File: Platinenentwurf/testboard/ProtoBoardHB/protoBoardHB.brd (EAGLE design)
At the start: 73.3 x 76.2 mm, 50 parts, among them IC1 CD74HCT125M, J1 M20-9980545, J2 M20-9980545, Q1 SMMBT3904WT1G, U2 STM32F4X5RG

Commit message: änderungen Platine + Bestellliste
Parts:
- added J3, J4: M20-9990246, SamacSys_Parts:HDRV2W64P0X254_1X2_508X254X864
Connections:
- new net N$2: HB_2.6, J3.2
- new net N$7: HB_1.6, J4.1
- net IS_1: now also J4.2; no longer HB_1.6
- net IS_2: now also J3.1; no longer HB_2.6
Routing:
- net GND: track 427.1 -> 482.9 mm, vias 8 -> 13
- net N$7: track 0.00 -> 24.3 mm, vias 0 -> 1
- net N$2: track 0.00 -> 23.4 mm, vias 0 -> 1
- net IS_1: track 75.8 -> 90.4 mm, vias 3 -> 2
- net IS_2: track 63.4 -> 67.3 mm, vias 3 -> 2

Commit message: update Platine
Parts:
- removed CAN_CONNECTION: 282836-2, SamacSys_Parts:SHDR2W100P0X500_1X2_1000X820X1
- removed C_HB_VS_1, C_HB_VS_2: 0.47uF, adafruit:C1206
- removed C_Q_1, C_Q_2: 22pF, adafruit:C0805
- removed C_VCAP_1, C_VCAP_2: 2.2uF, adafruit:C1206
- removed C_VDDA, C_VDD_1, C_VDD_2, C_VDD_3, C_VDD_4: 100nF, adafruit:C1206
- removed C_VDD_47: 4.7nF, adafruit:C1206
- removed C_VR33_VIN, C_VR5_VIN: 1uF, adafruit:C1206
- removed C_VR33_VO1, C_VR5_VO1: 4.7uF, adafruit:C1206
- removed IC1: CD74HCT125M, SamacSys_Parts:SOIC127P600X175-14N
- removed J1, J2: M20-9980545, SamacSys_Parts:HDRV10W80P254_2X5_1270X508X864
- removed J3, J4: M20-9990246, SamacSys_Parts:HDRV2W64P0X254_1X2_508X254X864
- removed QUARZ: ABLS-8.000MHZ-K4T, SamacSys_Parts:ABLS-12.000MHZ-B2
- removed R_CD: 1K, adafruit:R1206
- removed R_HB_INH_1, R_HB_INH_2, R_HB_IN_1, R_HB_IN_2: 10K, adafruit:R1206
- removed R_HB_IS_1, R_HB_IS_2: 1k, adafruit:R1206
- removed R_SMM_1, R_SMM_2: 100K, adafruit:R1206
- removed VREG_55: LDL1117S50R, SamacSys_Parts:SOT230P700X180-4N
- added C1, C3: 4.7uF, adafruit:C1206
- added C10, C12, C7, C8, C9: 100nF, adafruit:C1206
- added C11: 4.7nF, adafruit:C1206
- added C2, C4: 1uF, adafruit:C1206
- added C5, C6: 2.2uF, adafruit:C1206
- added CAN_OUT: 282836-2, SamacSys_Parts:SHDR2W100P0X500_1X2_1000X820X1
- added CD74HCT: CD74HCT125M, SamacSys_Parts:SOIC127P600X175-14N
- added CH1, CH2: 0.47uF, adafruit:C1206
- added CQ1, CQ2: 22pF, adafruit:C0805
- added J_CD, SENSORIK: M20-9980545, SamacSys_Parts:HDRV10W80P254_2X5_1270X508X864
- added J_IS1, J_IS2: M20-9990246, SamacSys_Parts:HDRV2W64P0X254_1X2_508X254X864
- added QUARTZ: ABLS-8.000MHZ-K4T, SamacSys_Parts:ABLS-12.000MHZ-B2
- added R10, R11, R12, R13: 10K, adafruit:R1206
- added R14, R9: 1k, adafruit:R1206
- added R15: 1K, adafruit:R1206
- added R16: 100K, adafruit:R1206
- added R17: 7.5K, adafruit:R1206
- added VREG_5: LDL1117S50R, SamacSys_Parts:SOT230P700X180-4N
- moved C_CAN 2.01 mm to (64.1, 34.9)
- moved CAN_T 2.01 mm to (64.1, 29.8)
- moved Q1 2.01 mm to (64.1, 17.1)
- moved HB_1 2.01 mm to (13.3, 52.7)
- moved U2 2.01 mm to (52.7, 34.9)
- moved BAT 2.01 mm to (8.26, 38.7)
- moved HB_ST 2.01 mm to (45.1, 56.5)
- moved R3 2.01 mm to (45.1, 23.5)
- moved R4 2.01 mm to (47.6, 23.5)
- moved R5 2.01 mm to (50.2, 23.5)
- moved R6 2.01 mm to (52.7, 23.5)
- moved SWD 2.01 mm to (69.2, 59.1)
- moved HB_2 2.01 mm to (29.8, 52.7)
- moved R1 2.01 mm to (31.1, 17.1)
- moved R2 2.01 mm to (28.6, 17.1)
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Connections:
- removed net N$16: J2.8
- removed net N$17: J2.10
- net CANH: now also CAN_OUT.1; no longer CAN_CONNECTION.1
- net CANL: now also CAN_OUT.2; no longer CAN_CONNECTION.2
- net CD_EN: now also CD74HCT.1, CD74HCT.13, CD74HCT.4, J_CD.7, J_CD.9; no longer IC1.1, IC1.13, IC1.4, J1.7, J1.9
- net CD_VCC: now also CD74HCT.14, J_CD.1, J_CD.3; no longer IC1.14, J1.1, J1.3
- net GND: now also C1.2, C10.2, C11.2, C12.2, C2.2, C3.1, C4.1, C5.2, C6.2, C7.2, C8.2, C9.2, CD74HCT.7, CH1.2, CH2.2, CQ1.2, CQ2.2, R14.1, R15.1, R17.2, R9.1, SENSORIK.4, VREG_5.1; no longer C_HB_VS_1.2, C_HB_VS_2.2, C_Q_1.2, C_Q_2.2, C_VCAP_1.2, C_VCAP_2.2, C_VDDA.2, C_VDD_1.2, C_VDD_2.2, C_VDD_3.2, C_VDD_4.2, C_VDD_47.2, C_VR33_VIN.2, C_VR33_VO1.2, C_VR5_VIN.1, C_VR5_VO1.1, IC1.7, J2.4, R_CD.1, R_HB_IS_1.1, R_HB_IS_2.1, R_SMM_2.2, VREG_55.1
- net INH: now also CD74HCT.11, R11.1, R12.1; no longer IC1.11, R_HB_INH_1.1, R_HB_INH_2.1
- net INH_M: now also CD74HCT.12; no longer IC1.12
- net IN_1: now also CD74HCT.6, R13.1; no longer IC1.6, R_HB_IN_1.1
- net IN_2: now also CD74HCT.3, R10.1; no longer IC1.3, R_HB_IN_2.1
- net IN_M_1: now also CD74HCT.5; no longer IC1.5
- net IN_M_2: now also CD74HCT.2; no longer IC1.2
- net IS_1: now also J_IS1.2, R14.2; no longer J4.2, R_HB_IS_1.2
- net IS_2: now also J_IS2.1, R9.2; no longer J3.1, R_HB_IS_2.2
- net N$1: now also J_CD.10, R15.2; no longer J1.10, R_CD.2
- net N$15: now also SENSORIK.6; no longer J2.6
- net N$2: now also J_IS2.2; no longer J3.2
- net N$3: now also R13.2; no longer R_HB_IN_1.2
- net N$4: now also R12.2; no longer R_HB_INH_1.2
- net N$5: now also R10.2; no longer R_HB_IN_2.2
- net N$6: now also R11.2; no longer R_HB_INH_2.2
- net N$7: now also J_IS1.1; no longer J4.1
- net OSC_IN: now also CQ2.1, QUARTZ.2; no longer C_Q_2.1, QUARZ.2
- net OSC_OUT: now also CQ1.1, QUARTZ.1; no longer C_Q_1.1, QUARZ.1
- net OUT_PA4: now also SENSORIK.7; no longer J2.7
- net OUT_PA5: now also SENSORIK.3; no longer J2.3
- net OUT_PA6: now also SENSORIK.5; no longer J2.5
- net OUT_PB1: now also SENSORIK.1; no longer J2.1
- net PA8: now also R16.2; no longer R_SMM_1.2
- net SS_VN: now also R17.1, SENSORIK.2; no longer J2.2, R_SMM_2.1
- net V12: now also C2.1, C4.2, CH1.1, CH2.1, VREG_5.3; no longer C_HB_VS_1.1, C_HB_VS_2.1, C_VR33_VIN.1, C_VR5_VIN.2, VREG_55.3
- net V33: now also C1.1, C10.1, C11.1, C12.1, C5.1, C6.1, C7.1, C8.1, C9.1, CD74HCT.10, J_CD.2, J_CD.8, R16.1, SENSORIK.9; no longer C_VCAP_1.1, C_VCAP_2.1, C_VDDA.1, C_VDD_1.1, C_VDD_2.1, C_VDD_3.1, C_VDD_4.1, C_VDD_47.1, C_VR33_VO1.1, IC1.10, J1.2, J1.8, J2.9, R_SMM_1.1
- net V5: now also C3.2, J_CD.4, VREG_5.4; no longer C_VR5_VO1.2, J1.4, VREG_55.4
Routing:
- net GND: track 482.9 -> 495.0 mm, vias 13 -> 15
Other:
- board text added: "CD_EN"
- board text added: "CD_VCC"
- board text added: "GND"
- board text added: "INH_EXT"
- board text added: "IN_M_1"
- board text added: "IN_M_2"
- board text added: "IS_1"
- board text added: "IS_2"
- board text added: "NRST"
- board text added: "NU"
- board text added: "OUT_PA4"
- board text added: "OUT_PA5"
- board text added: "OUT_PA6"
- board text added: "OUT_PB1"
- board text added: "Protoboard"
- board text added: "SS_VN"
- board text added: "SWCLK"
- board text added: "SWDIO"
- board text added: "TRACESWO"
- board text added: "V33"
- board text added: "V5"

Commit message: Platinenupdate
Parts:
- removed CH2: 0.47uF, adafruit:C1206
- added C13: 470uF, adafruit:C050-075X075
- added C14, C15: 1nF, adafruit:C1206
- added CH3: 0.47uF, adafruit:C1206
- added MGT1: BEAGLEBONEBLACK_MOUNTING_HOLE, BeagleBone_Black_Wireless:BEAGLEBONEBLACK_MOUNTING_HOLE
- added R18, R19: 1k, adafruit:R1206
- moved J_IS1 31.9 mm to (21.0, 31.8), turned to 0 degrees
- moved J_IS2 9.44 mm to (46.4, 53.3), turned to 180 degrees
- moved R7 5.08 mm to (60.3, 23.5)
- moved R8 5.08 mm to (62.9, 23.5)
- moved VREG_33 5.08 mm to (40.0, 9.53)
- moved CD74HCT 5.08 mm to (33.7, 26.0)
- moved CH1 5.08 mm to (23.5, 24.8)
- moved J_CD 5.08 mm to (22.2, 19.7)
- moved R1 5.08 mm to (36.2, 17.1)
- moved R2 5.08 mm to (33.7, 17.1)
- moved VREG_5 5.08 mm to (26.0, 9.53)
- moved BAT 5.08 mm to (13.3, 38.7)
- moved R13 5.08 mm to (15.9, 24.8)
- moved R15 5.08 mm to (12.1, 12.1)
- moved C1 5.08 mm to (42.5, 17.1)
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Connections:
- new net BOOT0: R19.2, U2.60
- new net BOOT1: R18.2, U2.28
- net GND: now also C13.2, C14.2, C15.2, CH3.2, MGT1.P$1, R18.1, R19.1; no longer CH2.2
- net IS_1: no longer R14.2
- net IS_2: no longer R9.2
- net N$2: now also C15.1, R9.2
- net N$7: now also C14.1, R14.2
- net V12: now also C13.1, CH3.1; no longer CH2.1
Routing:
- net GND: track 495.0 -> 434.2 mm, vias 15 -> 14
- net IS_1: track 90.4 -> 57.1 mm
- net IS_2: track 67.2 -> 36.7 mm, vias 2 -> 1
- net V12: track 138.6 -> 158.9 mm
- net BOOT1: track 0.00 -> 12.1 mm, vias 0 -> 2
- net N$2: track 23.4 -> 33.8 mm, vias 1 -> 2
- net BOOT0: track 0.00 -> 8.77 mm, vias 0 -> 2
- net N$7: track 24.3 -> 32.0 mm, vias 1 -> 2
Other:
- board size 73.3 x 76.2 mm -> 78.3 x 76.2 mm

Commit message: Bestellistenupdate
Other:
- board size 78.3 x 76.2 mm -> 80 x 76 mm
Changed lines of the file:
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@@
 <setting verticaltext="up"/>
 </settings>
-<grid distance="25" unitdist="mil" unit="mil" style="lines" multiple="1" display="yes" altdistance="5" altunitdist="mil" altunit="mil"/>
+<grid distance="1" unitdist="mm" unit="mm" style="lines" multiple="1" display="yes" altdistance="5" altunitdist="mil" altunit="mil"/>
 <layers>
 <layer number="1" name="Top" color="4" fill="1" visible="yes" active="yes"/>
@@
 <layer number="18" name="Vias" color="2" fill="1" visible="yes" active="yes"/>
 <layer number="19" name="Unrouted" color="6" fill="1" visible="yes" active="yes"/>
-<layer number="20" name="Dimension" color="24" fill="1" visible="no" active="yes"/>
+<layer number="20" name="Dimension" color="24" fill="1" visible="yes" active="yes"/>
 <layer number="21" name="tPlace" color="7" fill="1" visible="yes" active="yes"/>
 <layer number="22" name="bPlace" color="7" fill="1" visible="no" active="yes"/>
@@
 <board>
 <plain>
-<wire x1="0.08" y1="0" x2="78.41" y2="0" width="0" layer="20"/>
-<wire x1="78.41" y1="0" x2="78.41" y2="76.19" width="0" layer="20"/>
-<wire x1="78.41" y1="76.19" x2="0.08" y2="76.19" width="0" layer="20"/>
-<wire x1="0.08" y1="76.19" x2="0.08" y2="0" width="0" layer="20"/>
+<wire x1="0" y1="0" x2="80" y2="0" width="0" layer="20"/>
+<wire x1="80" y1="0" x2="80" y2="76" width="0" layer="20"/>
+<wire x1="80" y1="76" x2="0" y2="76" width="0" layer="20"/>
+<wire x1="0" y1="76" x2="0" y2="0" width="0" layer="20"/>
 <wire x1="41.275" y1="19.685" x2="41.275" y2="14.605" width="0.1524" layer="21"/>
 <wire x1="41.275" y1="14.605" x2="43.815" y2="14.605" width="0.1524" layer="21"/>
@@
 <text x="16.8275" y="21.59" size="0.3048" layer="21">NU</text>
 <text x="16.8275" y="14.9225" size="0.3048" layer="21">NU</text>
-<text x="44.7675" y="54.2925" size="0.3048" layer="21">IS_2</text>
-<text x="47.3075" y="54.2925" size="0.3048" layer="21">IS_1</text>
-<text x="49.53" y="54.2925" size="0.3048" layer="21">IN_M_2</text>
-<text x="52.07" y="54.2925" size="0.3048" layer="21">IN_M_1</text>
-<text x="54.61" y="54.2925" size="0.3048" layer="21">INH_EXT</text>
-<text x="54.2925" y="60.96" size="0.3048" layer="21">INH_EXT</text>
-<text x="52.07" y="60.96" size="0.3048" layer="21">GND</text>
-<text x="49.8475" y="60.96" size="0.3048" layer="21">V33</text>
-<text x="47.3075" y="60.96" size="0.3048" layer="21">NU</text>
-<text x="44.7675" y="60.96" size="0.3048" layer="21">NU</text>
-<text x="58.42" y="54.2925" size="0.3048" layer="21">NRST</text>
-<text x="60.6425" y="54.2925" size="0.3048" layer="21">TRACESWO</text>
-<text x="63.5" y="54.2925" size="0.3048" layer="21">SWCLK</text>
-<text x="66.04" y="54.2925" size="0.3048" layer="21">SWDIO</text>
-<text x="68.8975" y="54.2925" size="0.3048" layer="21">V33</text>
-<text x="68.8975" y="60.96" size="0.3048" layer="21">V33</text>
+<text x="49.8475" y="54.2925" size="0.3048" layer="21">IS_2</text>
+<text x="52.3875" y="54.2925" size="0.3048" layer="21">IS_1</text>
+<text x="54.61" y="54.2925" size="0.3048" layer="21">IN_M_2</text>
+<text x="57.15" y="54.2925" size="0.3048" layer="21">IN_M_1</text>
+<text x="59.69" y="54.2925" size="0.3048" layer="21">INH_EXT</text>
+<text x="59.3725" y="60.96" size="0.3048" layer="21">INH_EXT</text>
+<text x="57.15" y="60.96" size="0.3048" layer="21">GND</text>
+<text x="54.9275" y="60.96" size="0.3048" layer="21">V33</text>
+<text x="52.3875" y="60.96" size="0.3048" layer="21">NU</text>
+<text x="49.8475" y="60.96" size="0.3048" layer="21">NU</text>
+<text x="63.5" y="54.2925" size="0.3048" layer="21">NRST</text>
+<text x="65.7225" y="54.2925" size="0.3048" layer="21">TRACESWO</text>
+<text x="68.58" y="54.2925" size="0.3048" layer="21">SWCLK</text>
+<text x="71.12" y="54.2925" size="0.3048" layer="21">SWDIO</text>
+<text x="73.9775" y="54.2925" size="0.3048" layer="21">V33</text>
+<text x="73.9775" y="60.96" size="0.3048" layer="21">V33</text>
+<text x="71.4375" y="60.96" size="0.3048" layer="21">GND</text>
+<text x="68.8975" y="60.96" size="0.3048" layer="21">GND</text>
 <text x="66.3575" y="60.96" size="0.3048" layer="21">GND</text>
 <text x="63.8175" y="60.96" size="0.3048" layer="21">GND</text>
-<text x="61.2775" y="60.96" size="0.3048" layer="21">GND</text>
-<text x="58.7375" y="60.96" size="0.3048" layer="21">GND</text>
-<text x="43.4975" y="8.89" size="0.3048" layer="21">V33</text>
-<text x="45.4025" y="8.89" size="0.3048" layer="21">OUT_PA4</text>
-<text x="47.9425" y="8.89" size="0.3048" layer="21">OUT_PA6</text>
-<text x="50.4825" y="8.89" size="0.3048" layer="21">OUT_PA5</text>
-<text x="53.0225" y="8.89" size="0.3048" layer="21">OUT_PB1</text>
-<text x="53.34" y="2.2225" size="0.3048" layer="21">SS_VN</text>
-<text x="51.1175" y="2.2225" size="0.3048" layer="21">GND</text>
-<text x="48.5775" y="2.2225" size="0.3048" layer="21">NU</text>
-<text x="46.0375" y="2.2225" size="0.3048" layer="21">NU</text>
-<text x="43.4975" y="2.2225" size="0.3048" layer="21">NU</text>
+<text x="48.5775" y="8.89" size="0.3048" layer="21">V33</text>
+<text x="50.4825" y="8.89" size="0.3048" layer="21">OUT_PA4</text>
+<text x="53.0225" y="8.89" size="0.3048" layer="21">OUT_PA6</text>
+<text x="55.5625" y="8.89" size="0.3048" layer="21">OUT_PA5</text>
+<text x="58.1025" y="8.89" size="0.3048" layer="21">OUT_PB1</text>
+<text x="59.055" y="2.2225" size="0.3048" layer="21">SS_VN</text>
+<text x="56.8325" y="2.2225" size="0.3048" layer="21">GND</text>
+<text x="54.2925" y="2.2225" size="0.3048" layer="21">NU</text>
+<text x="51.7525" y="2.2225" size="0.3048" layer="21">NU</text>
+<text x="49.2125" y="2.2225" size="0.3048" layer="21">NU</text>
 <text x="51.435" y="71.12" size="2.54" layer="21">Protoboard</text>
 <hole x="45.43" y="57.88" drill="3.5"/>
@@
 <attribute name="MOUSER_PART_NUMBER" value="815-ABLS-8.0MK4-T" x="113.665" y="51.435" size="1.778" layer="27" rot="R90" display="off"/>
 <attribute name="MPN" value="ABLS-8.000MHZ-K4T" x="113.665" y="51.435" size="1.778" layer="27" rot="R90" display="off"/>
-<attribute name="NAME" x="42.126" y="32.47066875" size="1.27" layer="25" rot="R90" align="center"/>
+<attribute name="NAME" x="39.154" y="27.85433125" size="0.762" layer="25" rot="R270" align="center"/>
 <attribute name="OC_FARNELL" value="2467758" x="113.665" y="51.435" size="1.778" layer="27" rot="R90" display="off"/>
 <attribute name="VALUE" x="42.126" y="28.66066875" size="1.27" layer="27" rot="R90" align="center"/>

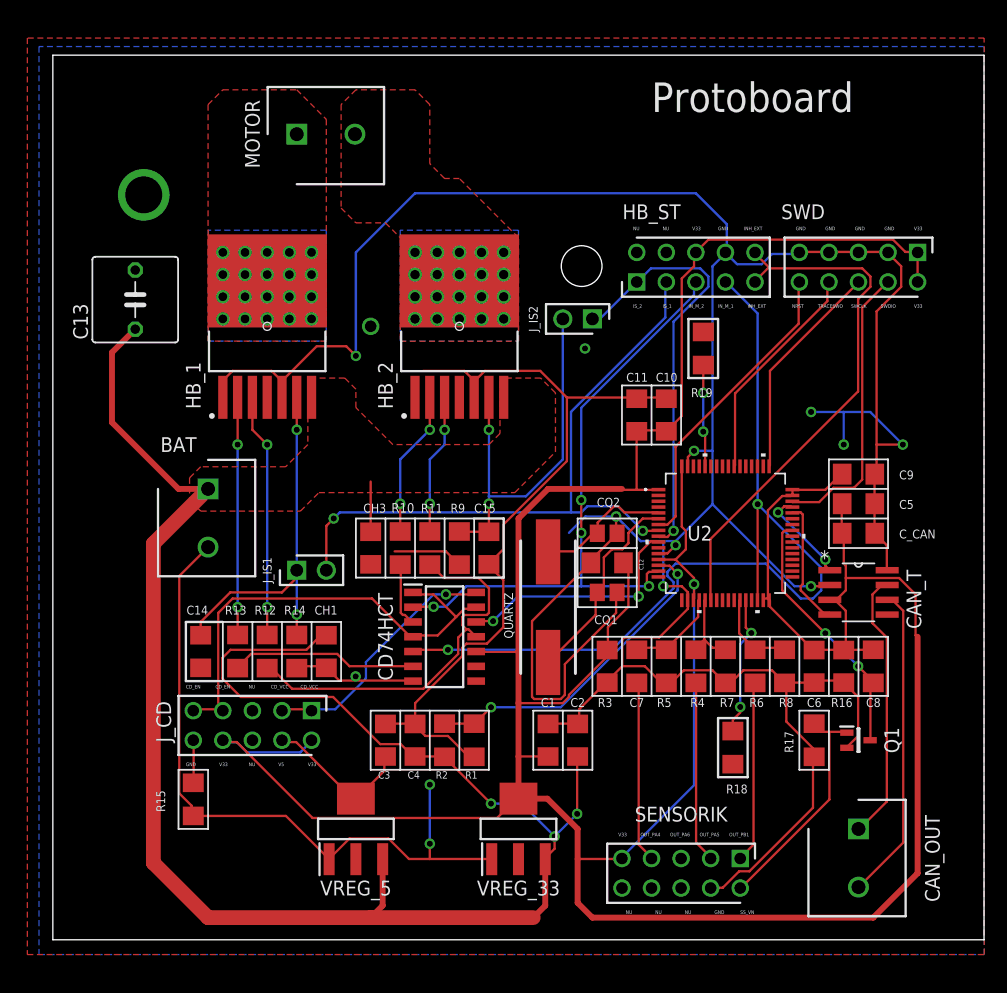
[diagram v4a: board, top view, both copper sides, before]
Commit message: Platinenupdate auf 0.7um Kupfer
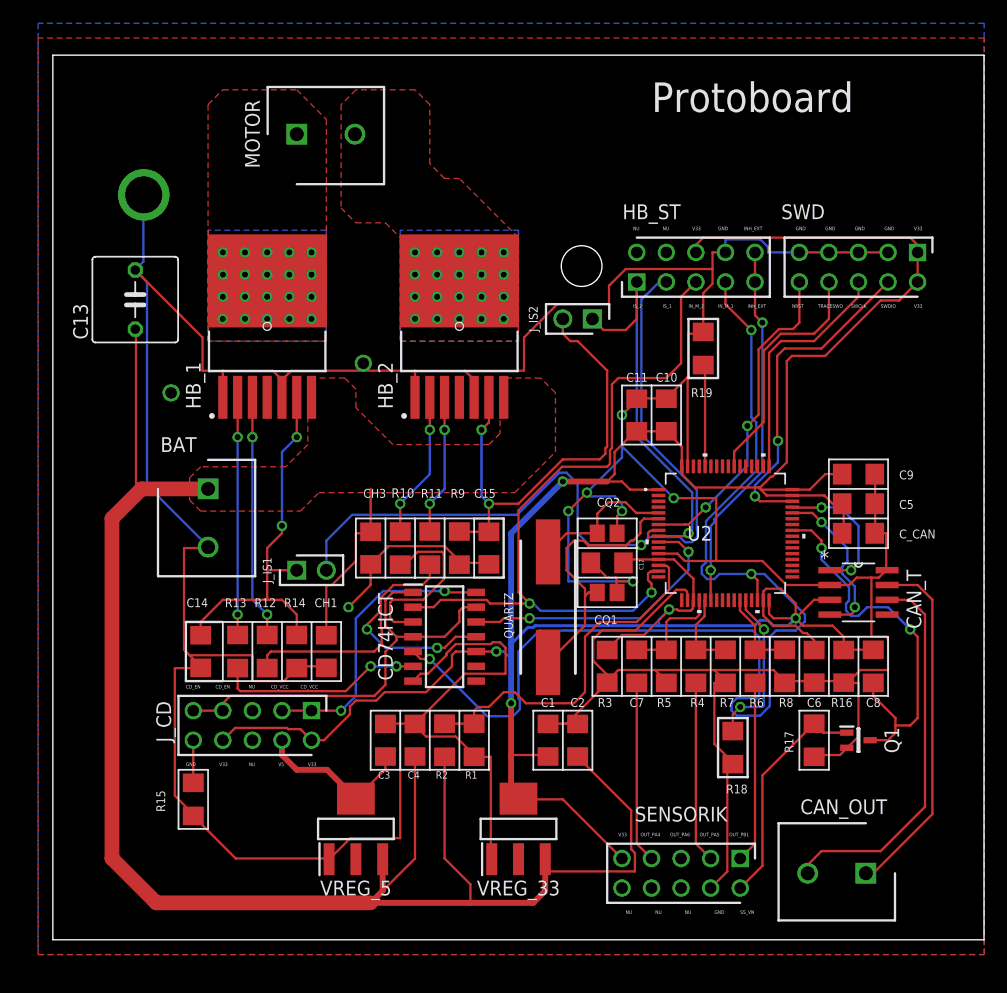
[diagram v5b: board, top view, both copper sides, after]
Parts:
- moved CAN_OUT 3.86 mm to (69.8, 5.71), turned to 180 degrees
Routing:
- net V33: track 306.2 -> 243.3 mm, vias 1 -> 5
- net IN_M_1: track 79.6 -> 101.9 mm, vias 2 -> 3
- net GND: track 434.2 -> 448.4 mm, vias 14 -> 9
- net INH_EXT: track 46.1 -> 32.0 mm, vias 0 -> 2
- net IS_1: track 57.1 -> 70.1 mm, vias 2 -> 1
- net PA8: track 22.2 -> 34.3 mm
- net IN_M_2: track 53.5 -> 63.5 mm, vias 4 -> 2
- net IN_2: track 5.52 -> 15.3 mm
- net CANH: track 23.3 -> 30.6 mm
- net N$2: track 33.8 -> 40.0 mm
- net CANL: track 27.1 -> 33.2 mm
- net OSC_OUT: track 17.6 -> 22.9 mm
- net CD_EN: track 41.3 -> 37.0 mm
- net CAN1_TX: track 8.27 -> 12.3 mm
- net INH_M: track 20.7 -> 24.6 mm
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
